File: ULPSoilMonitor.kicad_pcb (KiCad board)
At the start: 2 copper layers, 42.5 x 68.2 mm, 36 parts, among them J1 Conn_01x03_Male, J2 Conn_01x03_Male, J3 Conn_01x03_Male, J4 Conn_01x03_Male, J5 Conn_01x03_Male, J6 Conn_01x03_Male, J7 USB_B_Micro, Q1 BC807, Q2 MMDT3904, U1 ESP32-WROOM-32, U2 FT231XS

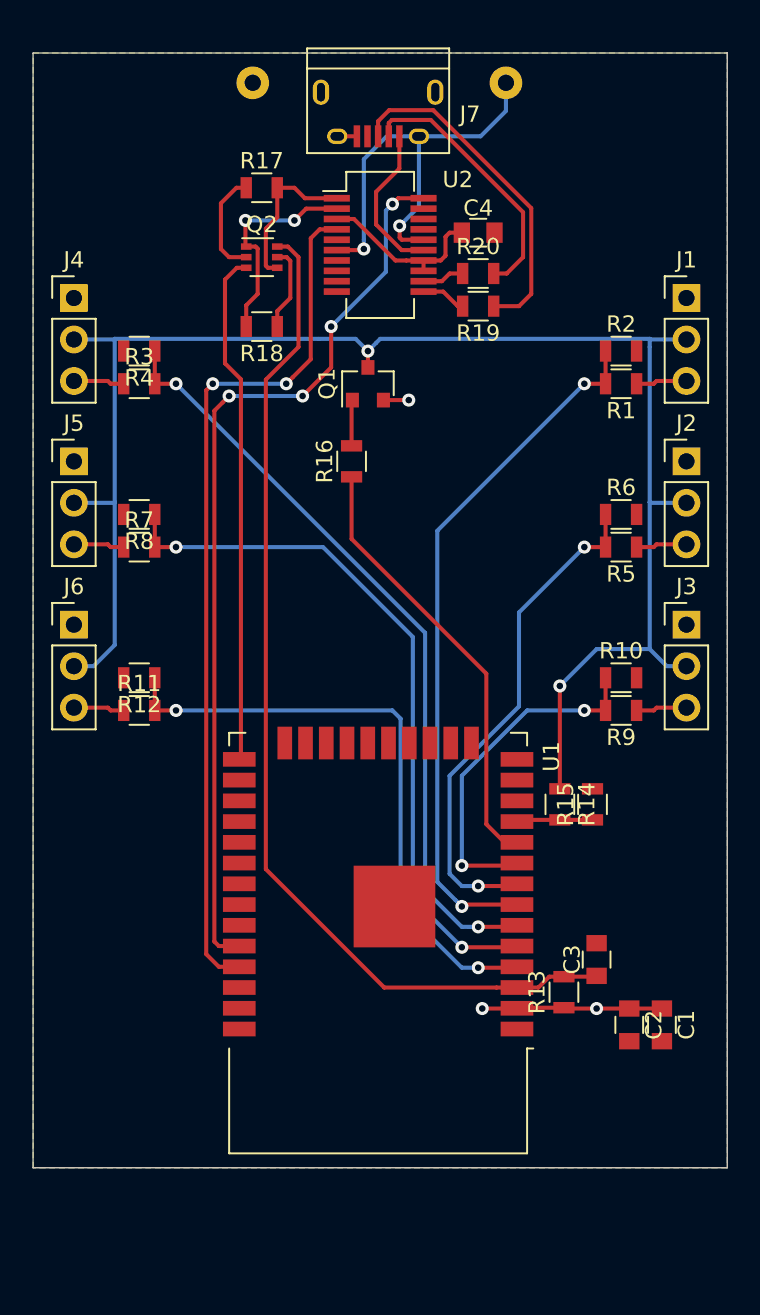
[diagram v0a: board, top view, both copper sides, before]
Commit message: update to use 18650 LiFePO4 cells
* connectors for one or two 18650 cells
* jumper to switch between battery & USB power
* add optional BME380
* reset push button
* more caps
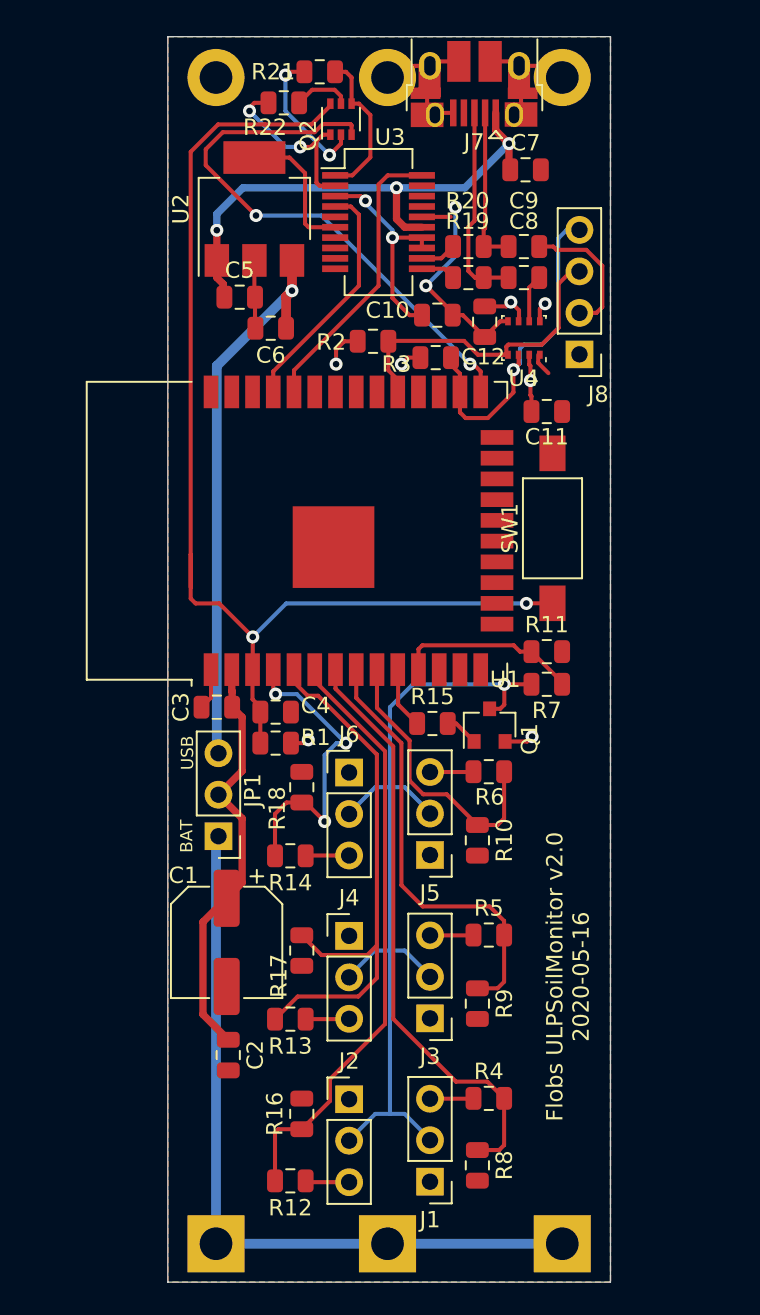
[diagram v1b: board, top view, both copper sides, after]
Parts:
- added C10: 100nF, Capacitor_SMD:C_0805_2012Metric, F.Cu at (55.0, 45.3)
- added C11: 100nF, Capacitor_SMD:C_0805_2012Metric, F.Cu at (61.7, 51.2)
- added C12: 100nF, Capacitor_SMD:C_0805_2012Metric, F.Cu at (57.9, 45.7)
- added C5: 330nF, Capacitor_SMD:C_0805_2012Metric, F.Cu at (42.9, 44.2)
- added C6: 100nF, Capacitor_SMD:C_0805_2012Metric, F.Cu at (44.8, 46.1)
- added C7: 10nF, Capacitor_SMD:C_0805_2012Metric, F.Cu at (60.4, 36.4)
- added C8: 47pF, Capacitor_SMD:C_0805_2012Metric, F.Cu at (60.3, 43.0)
- added C9: 47pF, Capacitor_SMD:C_0805_2012Metric, F.Cu at (60.3, 41.1)
- added J8: BME280_(GYBMEP), Connector_PinHeader_2.54mm:PinHeader_1x04_P2.54mm_Vertical, F.Cu at (63.7, 47.7)
- added JP1: Jumper_3_Bridged12, Connector_PinHeader_2.54mm:PinHeader_1x03_P2.54mm_Vertical, F.Cu at (41.6, 77.2)
- added R21: 10k, Resistor_SMD:R_0805_2012Metric, F.Cu at (47.8, 30.4)
- added R22: 10k, Resistor_SMD:R_0805_2012Metric, F.Cu at (45.6, 32.3)
- added SW1: RESET, Button_Switch_SMD:SW_SPST_FSMSM, F.Cu at (62.0, 58.4)
- added U3: FT231XS, Package_SO:QSOP-20_3.9x8.7mm_P0.635mm, F.Cu at (51.4, 39.6)
- added U4: BME280, Package_LGA:Bosch_LGA-8_2.5x2.5mm_P0.65mm_ClockwisePinNumbering, F.Cu at (60.3, 46.7)
- BT1: footprint flobs-KiCad-footprints:BH321-2P -> flobs-KiCad-footprints:BatteryHolder_BHC-18650-1P-2P
- C1: value 22μF -> 470μF; footprint Capacitors_SMD:C_0805 -> Capacitor_SMD:CP_Elec_6.3x7.7
- C2: value 100nF -> 22μF; footprint Capacitors_SMD:C_0805 -> Capacitor_SMD:C_0805_2012Metric
- C3: value 100μF -> 100nF; footprint Capacitors_SMD:C_0805 -> Capacitor_SMD:C_0805_2012Metric
- C4: footprint Capacitors_SMD:C_0805 -> Capacitor_SMD:C_0805_2012Metric
- J1, J2, J3, J4, J5, J6: footprint Pin_Headers:Pin_Header_Straight_1x03_Pitch2.54mm -> Connector_PinHeader_2.54mm:PinHeader_1x03_P2.54mm_Vertical
- J7: footprint Connect:USB_Micro-B -> Connector_USB:USB_Micro-B_Amphenol_10103594-0001LF_Horizontal
- Q1: footprint TO_SOT_Packages_SMD:SOT-23 -> Package_TO_SOT_SMD:SOT-23
- Q2: footprint TO_SOT_Packages_SMD:SOT-363_SC-70-6 -> Package_TO_SOT_SMD:SOT-363_SC-70-6
- R1: value 68k -> 10k; footprint Resistors_SMD:R_0805 -> Resistor_SMD:R_0805_2012Metric
- R10, R14, R19, R20, R5, R7, R8: footprint Resistors_SMD:R_0805 -> Resistor_SMD:R_0805_2012Metric
- R11, R9: value 68k -> 30k; footprint Resistors_SMD:R_0805 -> Resistor_SMD:R_0805_2012Metric
- R12, R4, R6: value 30k -> 68k; footprint Resistors_SMD:R_0805 -> Resistor_SMD:R_0805_2012Metric
- R13: value 10k -> 68k; footprint Resistors_SMD:R_0805 -> Resistor_SMD:R_0805_2012Metric
- R15: value 30k -> 3k9; footprint Resistors_SMD:R_0805 -> Resistor_SMD:R_0805_2012Metric
- R16: value 3k9 -> 30k; footprint Resistors_SMD:R_0805 -> Resistor_SMD:R_0805_2012Metric
- R17, R18: value 10k -> 30k; footprint Resistors_SMD:R_0805 -> Resistor_SMD:R_0805_2012Metric
- R2: value 30k -> 4k7; footprint Resistors_SMD:R_0805 -> Resistor_SMD:R_0805_2012Metric
- R3: value 68k -> 4k7; footprint Resistors_SMD:R_0805 -> Resistor_SMD:R_0805_2012Metric
- U2: value FT231XS -> UA7BM33; footprint Housings_SSOP:QSOP-20_3.9x8.7mm_Pitch0.635mm -> Package_TO_SOT_SMD:SOT-223-3_TabPin2
- moved BT1 71.1 mm to (52.0, 102.2), turned to 90 degrees
- moved J1 56.3 mm to (54.6, 98.4), turned to 180 degrees
- moved R4 50.5 mm to (58.2, 93.3), turned to 0 degrees
- moved R17 46.8 mm to (46.7, 84.2), turned to 270 degrees
- moved R8 44.9 mm to (57.5, 97.4), turned to 270 degrees
- moved J2 44.2 mm to (49.6, 93.3)
- moved J4 42.5 mm to (49.6, 83.3)
- moved R16 40.1 mm to (46.7, 94.2)
- moved J5 32.5 mm to (54.6, 78.4), turned to 180 degrees
- moved R12 32.2 mm to (46.0, 98.3)
- moved C4 31.9 mm to (45.1, 69.6)
- moved R1 30.5 mm to (45.1, 71.5)
- moved J3 28.8 mm to (54.6, 88.4), turned to 180 degrees
- moved R18 28.3 mm to (46.7, 74.2), turned to 90 degrees
- moved C3 27.9 mm to (41.5, 69.3), turned to 180 degrees
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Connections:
- C1 pad 1: +BATT -> VCC
- C2 pad 1: +BATT -> VCC
- C3 pad 1: EN -> VCC
- C4 pad 1: Net-(C4-Pad1) -> EN
- J2 pad 3: SENSOR1 -> SENSOR3
- J3 pad 3: SENSOR2 -> SENSOR1
- J4 pad 3: SENSOR3 -> SENSOR4
- J5 pad 3: SENSOR4 -> SENSOR2
- Q1 pad 2: +BATT -> VCC
- R1 pad 1: SENSOR0 -> VCC
- R1 pad 2: SENSOR0_SCALED -> EN
- R11 pad 1: SENSOR5 -> VCC_SCALED
- R11 pad 2: SENSOR5_SCALED -> -BATT
- R12 pad 1: SENSOR5_SCALED -> SENSOR3
- R12 pad 2: -BATT -> SENSOR3_SCALED
- R13 pad 1: +BATT -> SENSOR4
- R13 pad 2: EN -> SENSOR4_SCALED
- R14 pad 1: SENSOR_VCC -> SENSOR5
- R14 pad 2: BATT_SCALED -> SENSOR5_SCALED
- R15 pad 1: BATT_SCALED -> SENSOR_ENABLE
- R15 pad 2: -BATT -> Net-(Q1-Pad1)
- R16 pad 1: SENSOR_ENABLE -> SENSOR3_SCALED
- R16 pad 2: Net-(Q1-Pad1) -> -BATT
- R17 pad 1: Net-(Q2-Pad2) -> SENSOR4_SCALED
- R17 pad 2: DTR -> -BATT
- R18 pad 1: Net-(Q2-Pad5) -> SENSOR5_SCALED
- R18 pad 2: RTS -> -BATT
- R2 pad 1: SENSOR0_SCALED -> SCL
- R2 pad 2: -BATT -> VCC
- R3 pad 1: SENSOR3 -> SDA
- R3 pad 2: SENSOR3_SCALED -> VCC
- R4 pad 1: SENSOR3_SCALED -> SENSOR0
- R4 pad 2: -BATT -> SENSOR0_SCALED
- R6 pad 1: SENSOR1_SCALED -> SENSOR2
- R6 pad 2: -BATT -> SENSOR2_SCALED
- R7 pad 1: SENSOR4 -> SENSOR_VCC
- R7 pad 2: SENSOR4_SCALED -> VCC_SCALED
- R8 pad 1: SENSOR4_SCALED -> SENSOR0_SCALED
- R9 pad 1: SENSOR2 -> SENSOR1_SCALED
- R9 pad 2: SENSOR2_SCALED -> -BATT
- U1 pad 11: BATT_SCALED -> VCC_SCALED
- U1 pad 2: +BATT -> VCC
- U1 pad 26: (no net) -> SDA
- U1 pad 29: (no net) -> SCL
- U2 pad 1: DTR -> VBUS
- U2 pad 2: RTS -> -BATT
- U2 pad 3: Net-(C4-Pad1) -> +3V3
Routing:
- net SENSOR_VCC: track 100.1 -> 55.6 mm, vias 2 -> 1
- net VCC: track 0.00 -> 40.5 mm, vias 0 -> 7
- net ESPTX: track 53.3 -> 14.7 mm, vias 2 -> 0
- net ESPRX: track 56.0 -> 17.7 mm, vias 4 -> 0
- net +3V3: track 0.00 -> 34.6 mm, vias 0 -> 1
- net +BATT: track 12.6 -> 46.2 mm, vias 3 -> 0
- net -BATT: track 28.2 -> 60.6 mm
- net SENSOR_ENABLE: track 27.0 -> 3.81 mm
- net VBUS: track 9.54 -> 32.5 mm, vias 0 -> 3
- net SDA: track 0.00 -> 21.4 mm, vias 0 -> 1
- net SCL: track 0.00 -> 19.9 mm
- net SENSOR5_SCALED: track 37.5 -> 19.1 mm, vias 2 -> 3
- net Net-(C10-Pad1): track 0.00 -> 13.3 mm, vias 0 -> 2
- net VCC_SCALED: track 0.00 -> 11.2 mm
- net Net-(C4-Pad1): track 10.7 -> 0.00 mm
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- added copper zone on B.Cu, net VCC
- removed copper zone on B.Cu, net +BATT
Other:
- board size 42.5 x 68.2 mm -> 27.1 x 76.2 mm
- board text added: "BAT"
- board text added: "Flobs ULPSoilMonitor v2.0 2020-05-16"
- board text added: "USB"

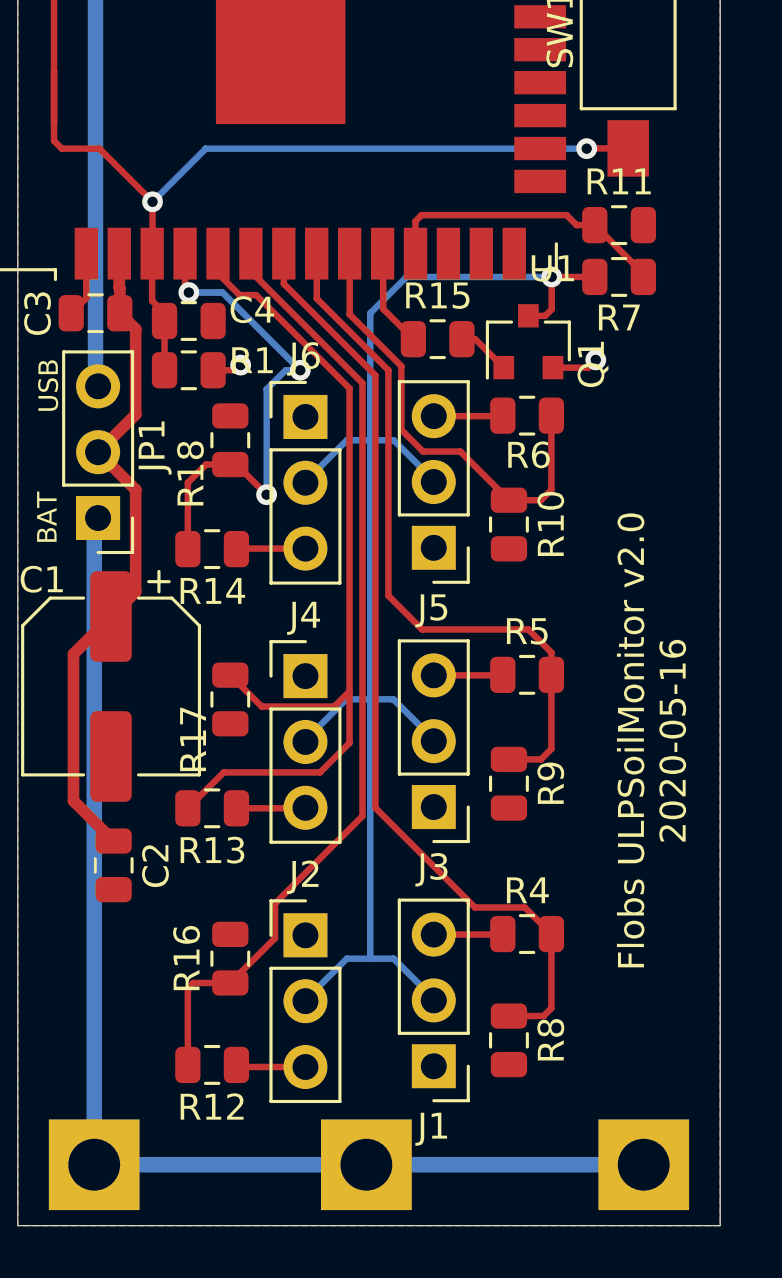
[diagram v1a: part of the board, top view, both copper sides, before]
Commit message: add additional spacing between sensor connectors
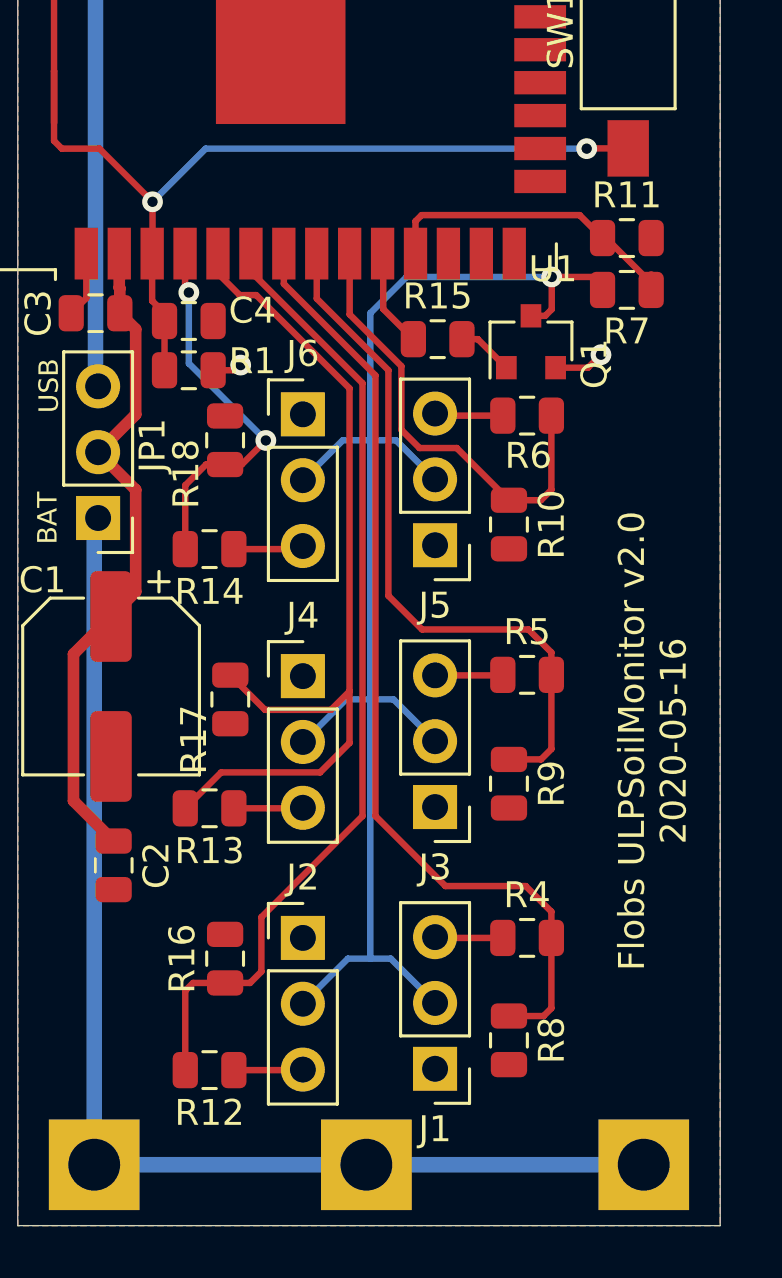
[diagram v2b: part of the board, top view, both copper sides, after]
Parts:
- moved R11 0.58 mm to (62.0, 66.4)
- moved R7 0.58 mm to (62.0, 68.4)
- moved R12 0.22 mm to (45.9, 98.5)
- moved R16 0.20 mm to (46.5, 94.2)
- moved R18 0.20 mm to (46.5, 74.2)
- moved R4 0.15 mm to (58.2, 93.4)
- moved J2 0.14 mm to (49.5, 93.4)
- moved J6 0.14 mm to (49.5, 73.2)
- moved J5 0.11 mm to (54.6, 78.2)
- moved J1 0.11 mm to (54.6, 98.5)
- moved J4 0.10 mm to (49.5, 83.3)
- moved R13 0.10 mm to (45.9, 88.4)
- moved R14 0.10 mm to (45.9, 78.4)
- moved Q1 0.10 mm to (58.3, 70.4)
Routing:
- net SENSOR5_SCALED: track 19.1 -> 14.8 mm, vias 3 -> 2
- net VCC_SCALED: track 11.2 -> 12.4 mm
- net SENSOR0_SCALED: track 36.3 -> 37.0 mm
- net SENSOR3_SCALED: track 36.7 -> 37.4 mm
